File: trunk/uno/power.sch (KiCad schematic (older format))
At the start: 16 parts, among them Q1 FDN340P, U1 NCP1117 5V, U2 LP2985-33DBVR, U5 LM358

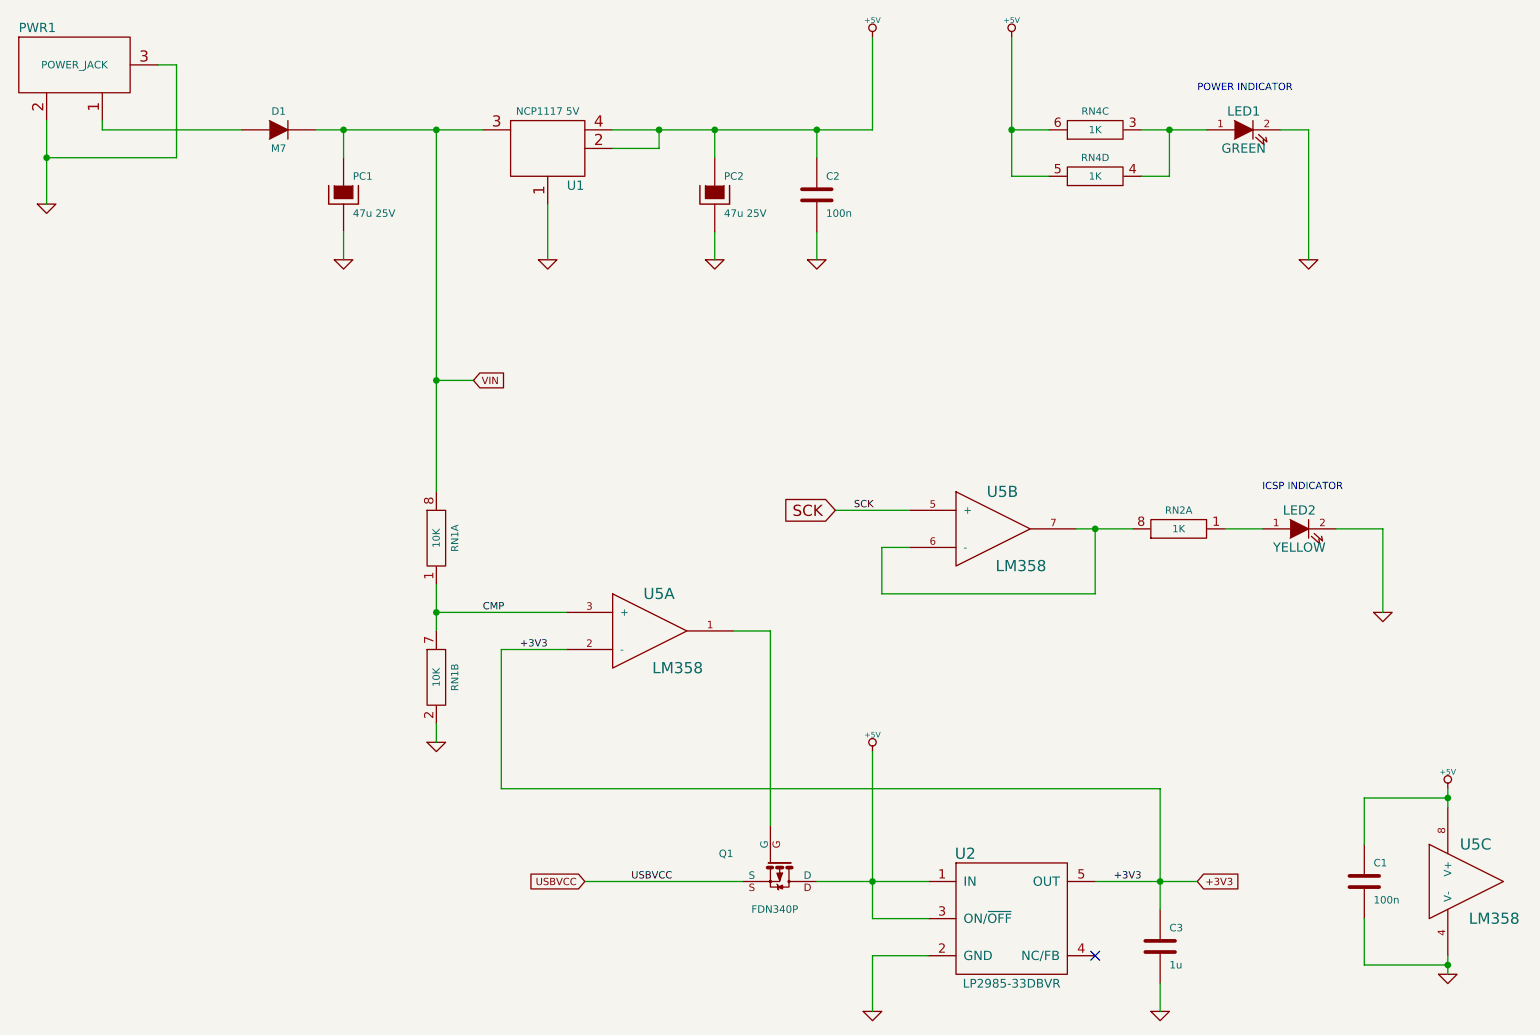
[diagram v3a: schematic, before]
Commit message: About half the comoponents placed, in the exact same location as the UNO Rev3 reference design, except I changed the USB socket to a mini.
A number of minor schematic errors were corrected, around the pin 
numbering of the four resistor network chips.
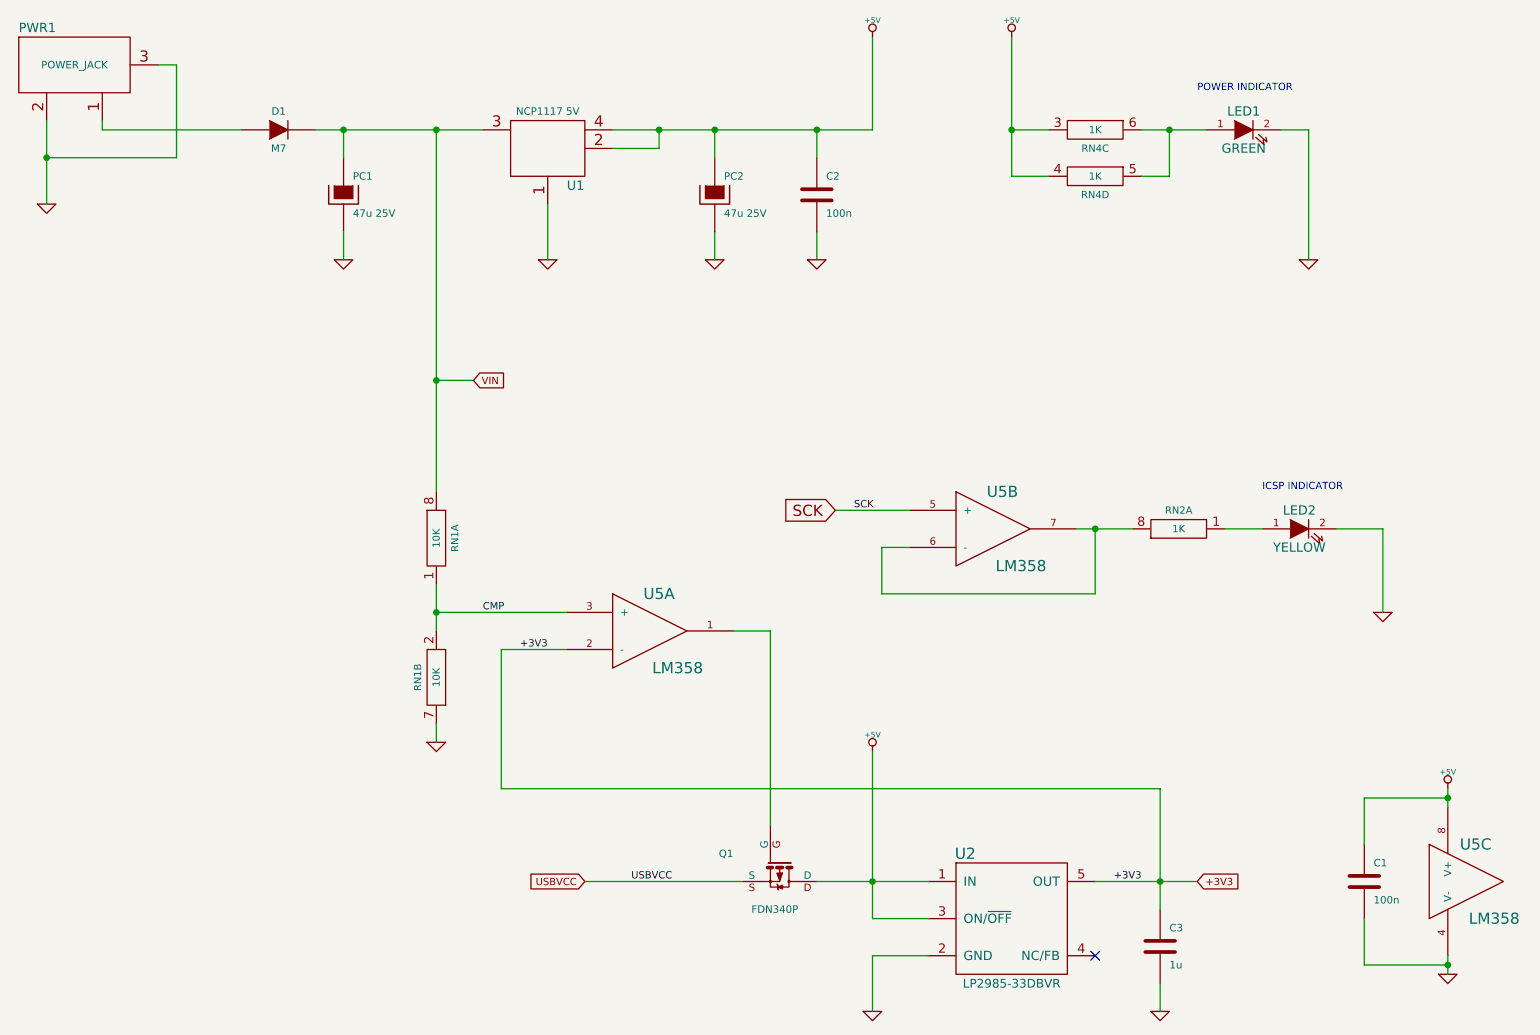
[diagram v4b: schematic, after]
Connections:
- net +5V: now also RN4.3, RN4.4 (3); no longer RN4.5 (6), RN4.6
- net CMP: now also RN1.2 (3); no longer RN1.7 (6)
- net GND: now also RN1.7 (6); no longer RN1.2 (3)
- new net: LED1.1 (A), RN4.5 (6), RN4.6
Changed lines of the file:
@@
 F 3 "" H 4200 4750 60  0000 C CNN
 	2    4200 4750
-	1    0    0    -1
+	-1   0    0    1
 $EndComp
 $Comp
@@
 F 3 "" H 7750 1800 60  0000 C CNN
 	3    7750 1800
-	0    -1   -1   0
+	0    1    1    0
 $EndComp
 $Comp
@@
 F 3 "" H 7750 2050 60  0000 C CNN
 	4    7750 2050
-	0    -1   -1   0
+	0    1    1    0
 $EndComp
 $EndSCHEMATC

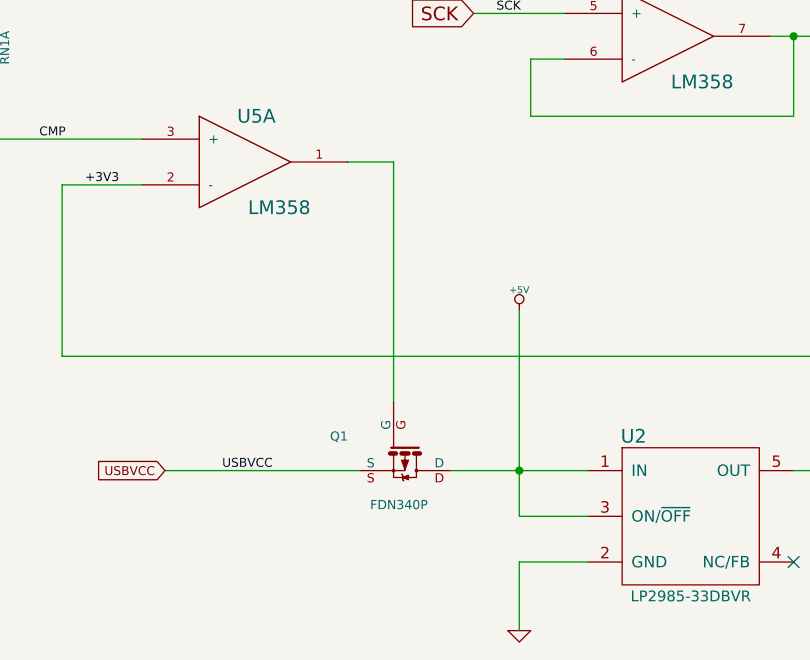
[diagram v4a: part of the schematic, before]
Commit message: All components placed. Some routing started.
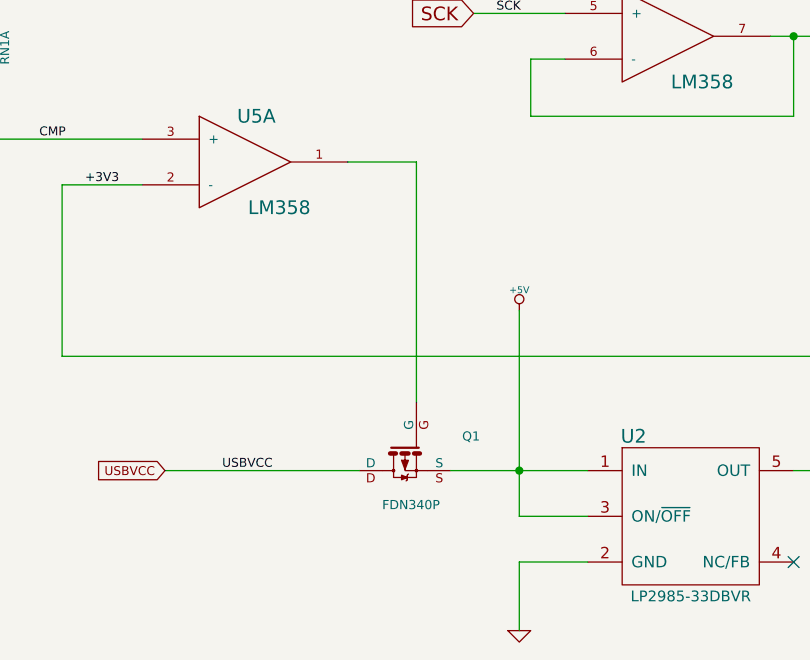
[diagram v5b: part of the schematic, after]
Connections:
- net +5V: now also Q1.S; no longer Q1.D
- net USBVCC: now also Q1.D; no longer Q1.S
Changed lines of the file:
@@
 Sheet 3 3
 Title "KiCADuino UNO Rev3"
-Date "25 jul 2013"
+Date "26 jul 2013"
 Rev "0.1"
 Comp "Gruvin & Co"
@@
 F 3 "~" H 6050 5750 60  0000 C CNN
 	1    6050 5750
-	0    1    1    0
+	0    -1   1    0
 $EndComp
 Wire Wire Line
@@
 Wire Wire Line
 	4550 4600 4900 4600
-Wire Wire Line
-	6000 5550 6000 4500
-Wire Wire Line
-	6000 4500 5800 4500
 Wire Wire Line
 	7300 1300 7300 2050
@@
 	0    1    1    0
 $EndComp
+Wire Wire Line
+	5800 4500 6100 4500
+Wire Wire Line
+	6100 4500 6100 5550
 $EndSCHEMATC
